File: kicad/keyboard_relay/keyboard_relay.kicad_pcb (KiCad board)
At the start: 2 copper layers, 155 x 90 mm, 24 parts, among them J3 Teensy_Header_24x1, J4 Teensy_Header_24x1, K1 HK19F-12V, K10 HK19F-12V, K11 HK19F-12V, K12 HK19F-12V, K13 HK19F-12V, K14 HK19F-12V, K15 HK19F-12V, K16 HK19F-12V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

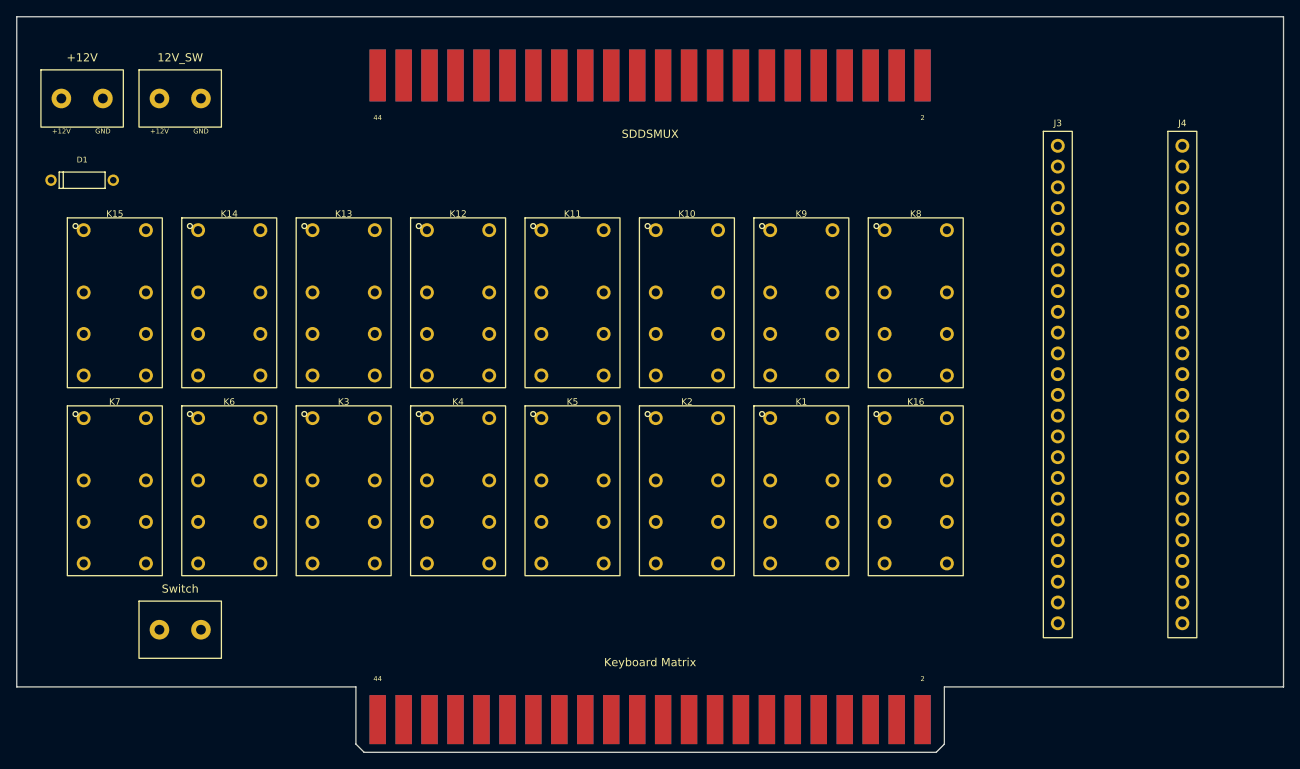
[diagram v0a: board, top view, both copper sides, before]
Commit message: latest kicad schematic and board layout.  Note the pcb needs routing, possibly using freerouting plugin.
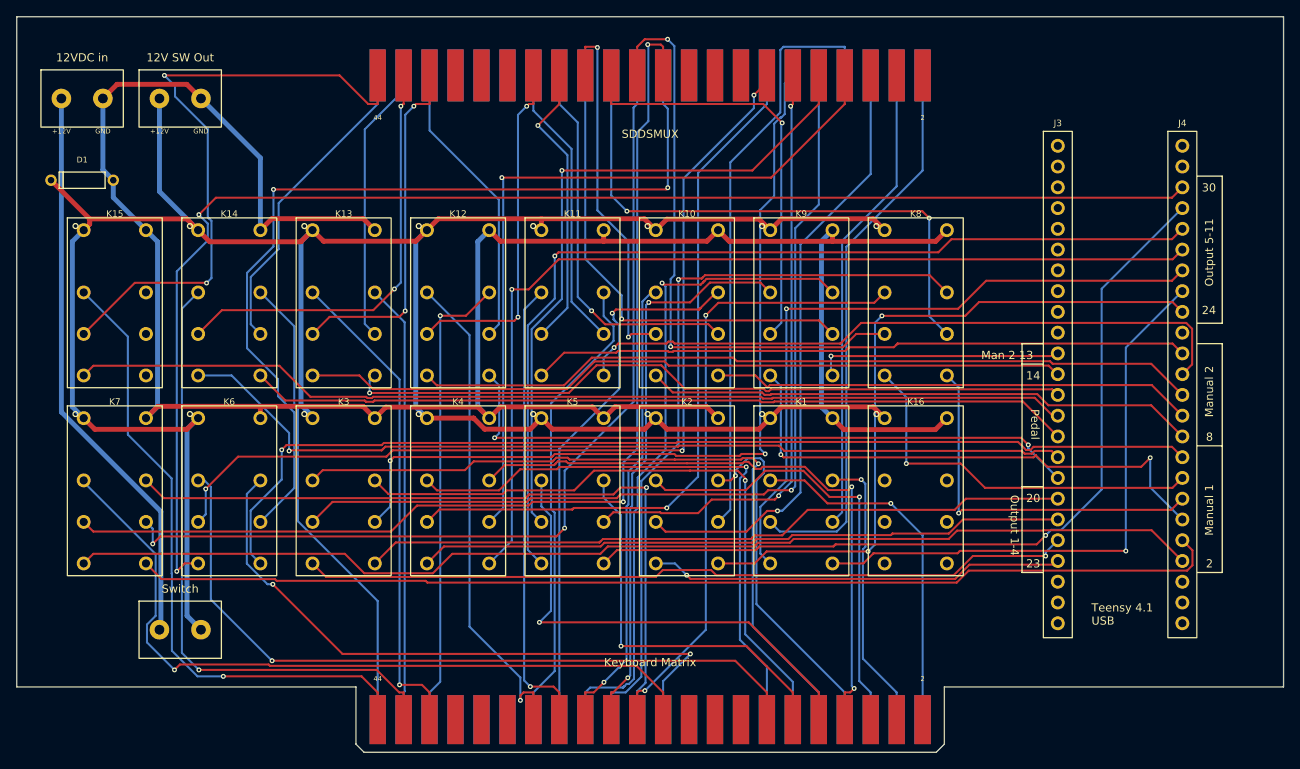
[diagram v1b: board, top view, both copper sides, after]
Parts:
- removed +12V, 12V_SW: 12V_Input, custom:ScrewTerminal_2P
- added 12V SW Out: 12V_Input, custom:ScrewTerminal_2P, F.Cu at (20.0, 10.0)
- added 12VDC in: 12V_Input, custom:ScrewTerminal_2P, F.Cu at (8.00, 10.0)
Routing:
- net COIL_12V_SW: track 0.00 -> 306.7 mm
- net COIL_GND: track 0.00 -> 290.7 mm
- net TEEN_30: track 0.00 -> 170.4 mm, vias 0 -> 2
- net TEEN_2: track 0.00 -> 139.9 mm
- net TEEN_3: track 0.00 -> 133.5 mm
- net COMP_22: track 0.00 -> 130.8 mm, vias 0 -> 2
- net TEEN_7: track 0.00 -> 127.7 mm, vias 0 -> 1
- net TEEN_16: track 0.00 -> 122.4 mm
- net TEEN_27: track 0.00 -> 118.7 mm, vias 0 -> 1
- net TEEN_28: track 0.00 -> 117.8 mm, vias 0 -> 1
- net COMP_14: track 0.00 -> 114.9 mm, vias 0 -> 3
- net COMP_23: track 0.00 -> 113.3 mm, vias 0 -> 2
- net COMP_9: track 0.00 -> 112.9 mm, vias 0 -> 1
- net TEEN_18: track 0.00 -> 111.7 mm, vias 0 -> 1
- net COMP_21: track 0.00 -> 108.5 mm, vias 0 -> 2
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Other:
- board text added: "14"
- board text added: "2"
- board text added: "20"
- board text added: "23"
- board text added: "24"
- board text added: "30"
- board text added: "8"
- board text added: "Man 2 13"
- board text added: "Manual 1"
- board text added: "Manual 2"
- board text added: "Output 1-4"
- board text added: "Output 5-11"
- board text added: "Pedal"
- board text added: "Teensy 4.1 USB"
